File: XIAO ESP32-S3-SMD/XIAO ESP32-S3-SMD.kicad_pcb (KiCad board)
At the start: 2 copper layers, 12 parts, among them J1 Conn_01x04_Socket, J2 Conn_01x03_Socket, J3 Conn_01x04_Socket, J4 Conn_01x03_Socket, J5 Conn_01x03_Socket, J6 Conn_01x02_Pin, U2 XIAO-ESP32-S3-SMD

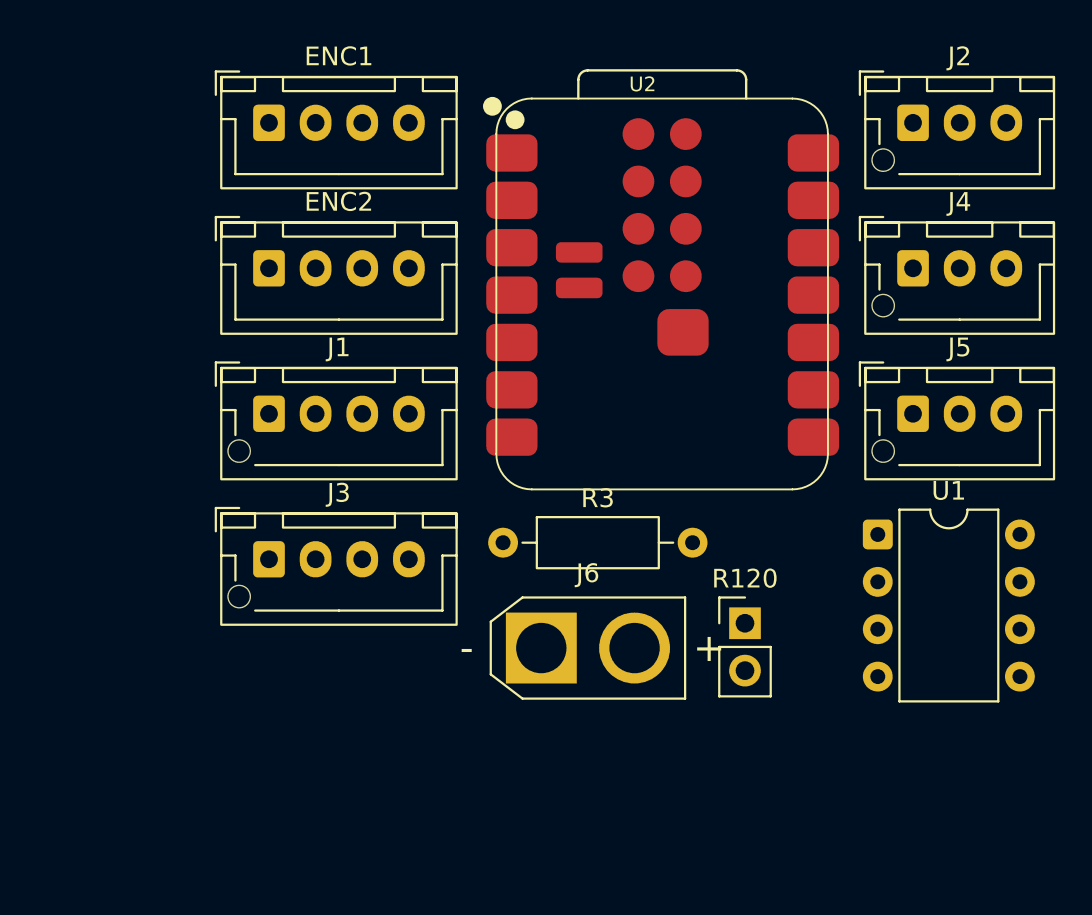
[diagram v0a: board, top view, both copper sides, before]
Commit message: XIAO S3の配置、配線前
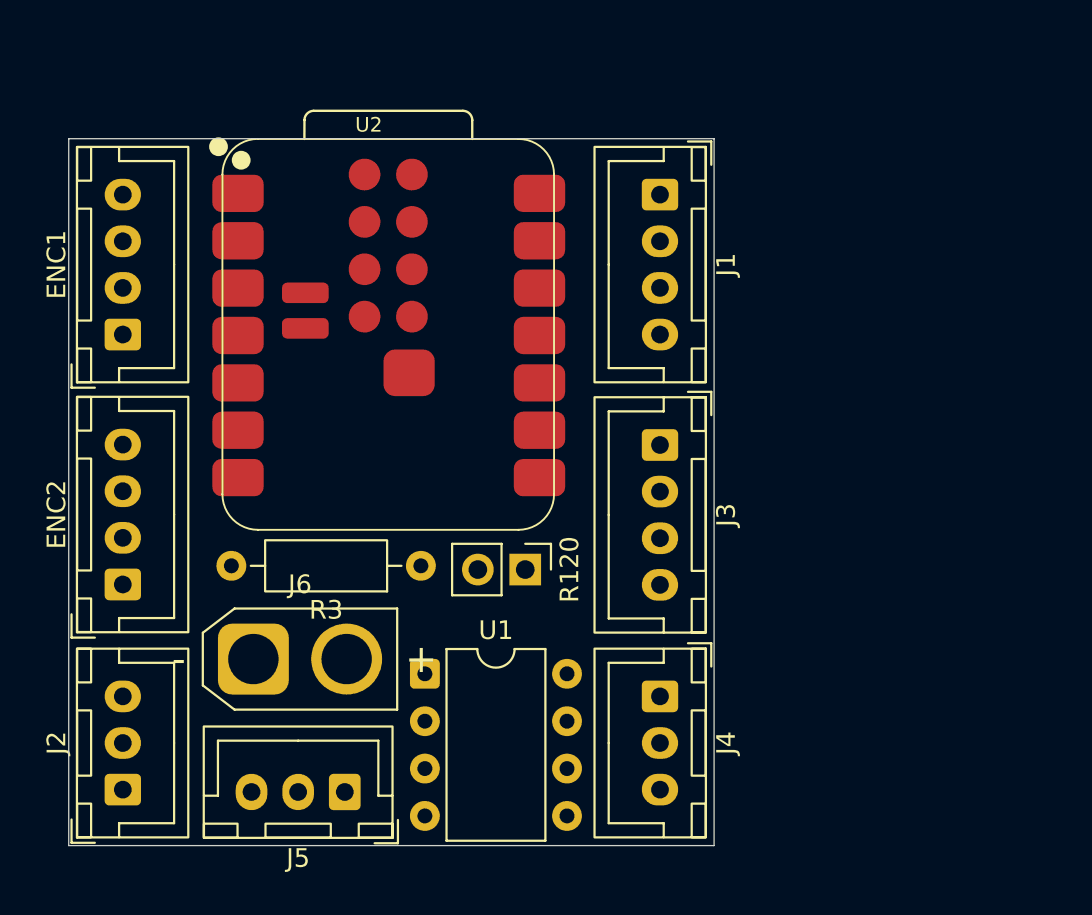
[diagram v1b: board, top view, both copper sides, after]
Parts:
- J1, J3: footprint Connector_JST:JST_XH_B4B-XH-AM_1x04_P2.50mm_Vertical -> Connector_JST:JST_XH_B4B-XH-A_1x04_P2.50mm_Vertical
- J2, J4, J5: footprint Connector_JST:JST_XH_B3B-XH-AM_1x03_P2.50mm_Vertical -> Connector_JST:JST_XH_B3B-XH-A_1x03_P2.50mm_Vertical
- moved J2 55.4 mm to (135.6, 97.3), turned to 90 degrees
- moved J5 36.6 mm to (147.5, 97.4), turned to 180 degrees
- moved J4 26.7 mm to (164.4, 92.3), turned to -90 degrees
- moved U1 25.4 mm to (151.8, 91.1)
- moved J1 24.0 mm to (164.4, 65.4), turned to -90 degrees
- moved J3 21.8 mm to (164.4, 78.8), turned to -90 degrees
- moved ENC2 18.7 mm to (135.6, 86.3), turned to 90 degrees
- moved J6 15.4 mm to (142.6, 90.3)
- moved U2 14.8 mm to (140.9, 83.5)
- moved ENC1 13.8 mm to (135.6, 72.9), turned to 90 degrees
- moved R120 12.1 mm to (157.2, 85.5), turned to -90 degrees
- moved R3 4.58 mm to (151.6, 85.3), turned to 180 degrees
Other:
- board outline added: 34.6 x 37.9 mm

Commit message: 電源ライン配線前
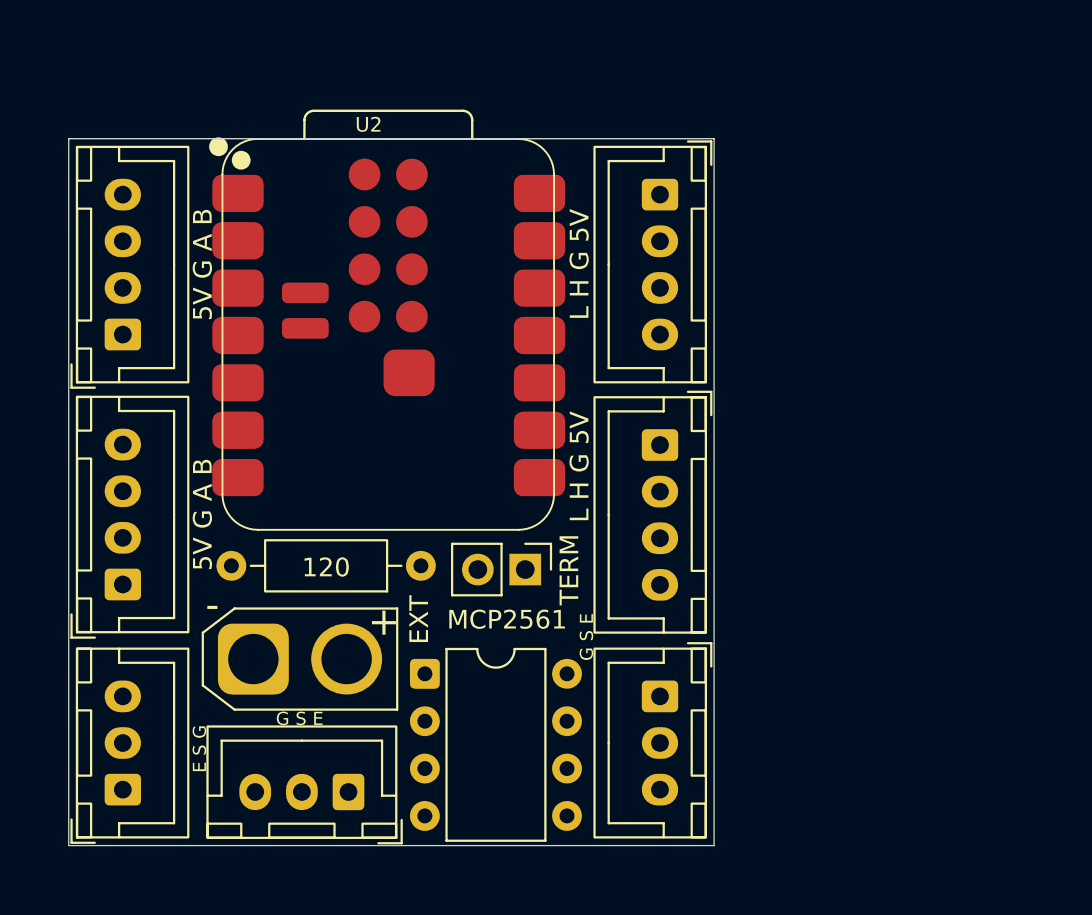
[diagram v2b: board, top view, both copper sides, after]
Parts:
- 5V G A B: renamed from ENC2
- 5V G A B: renamed from ENC1
- E S G: renamed from J2
- G S E: renamed from J5
- G S E: renamed from J4
- L H G 5V: renamed from J3
- L H G 5V: renamed from J1
- moved G S E 0.20 mm to (147.7, 97.4)
- renumbered R3 to 120, J6 to EXT, U1 to MCP2561, R120 to TERM
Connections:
- EXT pad 1: EXT_POWER -> GND
- EXT pad 2: GND -> EXT_POWER
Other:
- board text added: "CAN"
- board text added: "E S G"
- board text added: "ENC1"
- board text added: "ENC2"
- board text added: "G S E"
- board text added: "MULTI1"
- board text added: "MULTI2"
- board text added: "MULTI3"
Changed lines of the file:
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@@
 		(descr "8-lead though-hole mounted DIP package, row spacing 7.62mm (300 mils)")
 		(tags "THT DIP DIL PDIP 2.54mm 7.62mm 300mil")
-		(property "Reference" "U1"
-			(at 3.81 -2.33 0)
+		(property "Reference" "MCP2561"
+			(at 4.405 -2.89 0)
 			(layer "F.SilkS")
 			(effects
@@
 		(descr "Through hole straight pin header, 1x02, 2.54mm pitch, single row")
 		(tags "Through hole pin header THT 1x02 2.54mm single row")
-		(property "Reference" "R120"
+		(property "Reference" "TERM"
 			(at 0 -2.38 90)
 			(layer "F.SilkS")
@@
 		(descr "Connector XT30 Vertical Cable Male, https://www.tme.eu/Document/7d9d972ae3468777f69ec2ee99897652/XT30U-M.pdf")
 		(tags "RC Connector XT30")
-		(property "Reference" "J6"
-			(at 2.5 -4 0)
-			(layer "F.SilkS")
+		(property "Reference" "EXT"
+			(at 8.9 -2.1 90)
+			(layer "F.SilkS" knockout)
 			(effects
 				(font
@@
 		)
 		(fp_text user "-"
-			(at -4 0 0)
+			(at -2.2 -2.9 0)
 			(layer "F.SilkS")
 			(effects
@@
 		)
 		(fp_text user "+"
-			(at 9 0 0)
+			(at 7 -2 0)
 			(layer "F.SilkS")
 			(effects
@@
 			(remove_unused_layers no)
 			(roundrect_rratio 0.2)
-			(net "EXT_POWER")
+			(net "GND")
 			(pinfunction "Pin_1_1")
 			(pintype "passive")
@@
 			(layers "*.Cu" "*.Mask")
 			(remove_unused_layers no)
-			(net "GND")
+			(net "EXT_POWER")
 			(pinfunction "Pin_2_2")
 			(pintype "passive")
@@
 		(descr "JST XH series connector, B4B-XH-A (http://www.jst-mfg.com/product/pdf/eng/eXH.pdf)")
 		(tags "connector JST XH vertical")
-		(property "Reference" "J3"
-			(at 3.75 -3.55 90)
-			(layer "F.SilkS")
+		(property "Reference" "L H G 5V"
+			(at 1.17875 4.3 90)
+			(layer "F.SilkS" knockout)
 			(effects
 				(font
@@
 		(descr "JST XH series connector, B4B-XH-A (http://www.jst-mfg.com/product/pdf/eng/eXH.pdf)")
 		(tags "connector JST XH vertical")
-		(property "Reference" "ENC2"
-			(at 3.75 -3.55 90)
-			(layer "F.SilkS")
+		(property "Reference" "5V G A B"
+			(at 3.75 4.3 90)
+			(layer "F.SilkS" knockout)
 			(effects
 				(font
@@
 		(descr "JST XH series connector, B4B-XH-A (http://www.jst-mfg.com/product/pdf/eng/eXH.pdf)")
 		(tags "connector JST XH vertical")
-		(property "Reference" "J1"
-			(at 3.75 -3.55 90)
-			(layer "F.SilkS")
+		(property "Reference" "L H G 5V"
+			(at 3.75 4.3 90)
+			(layer "F.SilkS" knockout)
 			(effects
 				(font
@@
 		(descr "JST XH series connector, B4B-XH-A (http://www.jst-mfg.com/product/pdf/eng/eXH.pdf)")
 		(tags "connector JST XH vertical")
-		(property "Reference" "ENC1"
-			(at 3.75 -3.55 90)
-			(layer "F.SilkS")
+		(property "Reference" "5V G A B"
+			(at 3.75 4.3 90)
+			(layer "F.SilkS" knockout)
 			(effects
 				(font
@@
 	(footprint "Connector_JST:JST_XH_B3B-XH-A_1x03_P2.50mm_Vertical"
 		(layer "F.Cu")
-		(at 147.5 97.425 180)
+		(at 147.7 97.425 180)
 		(descr "JST XH series connector, B3B-XH-A (http://www.jst-mfg.com/product/pdf/eng/eXH.pdf)")
 		(tags "connector JST XH vertical")
-		(property "Reference" "J5"
-			(at 2.5 -3.55 0)
-			(layer "F.SilkS")
+		(property "Reference" "G S E"
+			(at 2.5 1.725 0)
+			(layer "F.SilkS" knockout)
+			(hide yes)
 			(effects
 				(font
@@
 		(descr "Resistor, Axial_DIN0207 series, Axial, Horizontal, pin pitch=10.16mm, 0.25W = 1/4W, length*diameter=6.3*2.5mm^2, http://cdn-reichelt.de/documents/datenblatt/B400/1_4W%23YAG.pdf")
 		(tags "Resistor Axial_DIN0207 series Axial Horizontal pin pitch 10.16mm 0.25W = 1/4W length 6.3mm diameter 2.5mm")
-		(property "Reference" "R3"
-			(at 5.08 -2.37 0)
+		(property "Reference" "120"
+			(at 5.08 -0.1 0)
 			(layer "F.SilkS")
 			(effects
@@
 		(descr "JST XH series connector, B3B-XH-A (http://www.jst-mfg.com/product/pdf/eng/eXH.pdf)")
 		(tags "connector JST XH vertical")
-		(property "Reference" "J4"
-			(at 2.5 -3.55 90)
-			(layer "F.SilkS")
+		(property "Reference" "G S E"
+			(at 2.5 1.8 90)
+			(layer "F.SilkS" knockout)
+			(hide yes)
 			(effects
 				(font
@@
 		(descr "JST XH series connector, B3B-XH-A (http://www.jst-mfg.com/product/pdf/eng/eXH.pdf)")
 		(tags "connector JST XH vertical")
-		(property "Reference" "J2"
-			(at 2.5 -3.55 90)
-			(layer "F.SilkS")
+		(property "Reference" "E S G"
+			(at 2.7 1.9 90)
+			(layer "F.SilkS" knockout)
+			(hide yes)
 			(effects
 				(font
@@
 		(layer "Edge.Cuts")
 	)
+	(gr_text "G S E"
+		(at 143.8 93.915 0)
+		(layer "F.SilkS" knockout)
+		(effects
+			(font
+				(size 0.7 0.7)
+				(thickness 0.1)
+			)
+			(justify left bottom)
+		)
+	)
+	(gr_text "E S G"
+		(at 140.14 96.4 90)
+		(layer "F.SilkS" knockout)
+		(effects
+			(font
+				(size 0.7 0.7)
+				(thickness 0.1)
+			)
+			(justify left bottom)
+		)
+	)
+	(gr_text "G S E"
+		(at 160.89 90.4 90)
+		(layer "F.SilkS" knockout)
+		(effects
+			(font
+				(size 0.7 0.7)
+				(thickness 0.1)
+			)
+			(justify left bottom)
+		)
+	)
+	(gr_text "MULTI3"
+		(at 145.3 95.7 0)
+		(layer "B.SilkS")
+		(effects
+			(font
+				(size 1 1)
+				(thickness 0.15)
+			)
+			(justify mirror)
+		)
+	)
+	(gr_text "MULTI1"
+		(at 137.4 94.5 90)
+		(layer "B.SilkS")
+		(effects
+			(font
+				(size 1 1)
+				(thickness 0.15)
+			)
+			(justify mirror)
+		)
+	)
+	(gr_text "ENC1"
+		(at 137.5 69.2 90)
+		(layer "B.SilkS")
+		(effects
+			(font
+				(size 1 1)
+				(thickness 0.15)
+			)
+			(justify mirror)
+		)
+	)
+	(gr_text "ENC2"
+		(at 137.6 82.5 90)
+		(layer "B.SilkS")
+		(effects
+			(font
+				(size 1 1)
+				(thickness 0.15)
+			)
+			(justify mirror)
+		)
+	)
+	(gr_text "CAN"
+		(at 162.6 69.1 90)
+		(layer "B.SilkS")
+		(effects
+			(font
+				(size 1 1)
+				(thickness 0.15)
+			)
+			(justify mirror)
+		)
+	)
+	(gr_text "CAN"
+		(at 162.6 82.4 90)
+		(layer "B.SilkS")
+		(effects
+			(font
+				(size 1 1)
+				(thickness 0.15)
+			)
+			(justify mirror)
+		)
+	)
+	(gr_text "MULTI2"
+		(at 162.6 94.8 90)
+		(layer "B.SilkS")
+		(effects
+			(font
+				(size 1 1)
+				(thickness 0.15)
+			)
+			(justify mirror)
+		)
+	)
 	(embedded_fonts no)

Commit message: 電源ラインの配線
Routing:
- net GND: track 0.00 -> 42.6 mm
- net EXT_POWER: track 0.00 -> 42.4 mm
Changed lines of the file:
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@@
 		)
 		(fp_text user "-"
-			(at -2.2 -2.9 0)
+			(at -2.4 -2.9 0)
 			(layer "F.SilkS")
 			(effects
@@
 		)
 	)
+	(segment
+		(start 137.6 90.3)
+		(end 135.6 92.3)
+		(width 2)
+		(layer "F.Cu")
+		(net "GND")
+	)
+	(segment
+		(start 142.6 90.3)
+		(end 137.6 90.3)
+		(width 2)
+		(layer "F.Cu")
+		(net "GND")
+	)
+	(segment
+		(start 142.73 93.63)
+		(end 142.7 93.6)
+		(width 2)
+		(layer "B.Cu")
+		(net "GND")
+	)
+	(segment
+		(start 151.795 93.63)
+		(end 142.73 93.63)
+		(width 2)
+		(layer "B.Cu")
+		(net "GND")
+	)
+	(segment
+		(start 164.4 97.3)
+		(end 162.8 97.3)
+		(width 2)
+		(layer "B.Cu")
+		(net "GND")
+	)
+	(segment
+		(start 142.7 93.6)
+		(end 142.7 90.4)
+		(width 2)
+		(layer "B.Cu")
+		(net "GND")
+	)
+	(segment
+		(start 158.91 91.09)
+		(end 156.37 93.63)
+		(width 2)
+		(layer "B.Cu")
+		(net "GND")
+	)
+	(segment
+		(start 142.7 97.425)
+		(end 142.7 93.6)
+		(width 2)
+		(layer "B.Cu")
+		(net "GND")
+	)
+	(segment
+		(start 142.7 90.4)
+		(end 142.6 90.3)
+		(width 0.2)
+		(layer "B.Cu")
+		(net "GND")
+	)
+	(segment
+		(start 160.54637 91.09)
+		(end 159.415 91.09)
+		(width 2)
+		(layer "B.Cu")
+		(net "GND")
+	)
+	(segment
+		(start 159.415 91.09)
+		(end 158.91 91.09)
+		(width 2)
+		(layer "B.Cu")
+		(net "GND")
+	)
+	(segment
+		(start 162.8 97.3)
+		(end 162.1 96.6)
+		(width 2)
+		(layer "B.Cu")
+		(net "GND")
+	)
+	(segment
+		(start 156.37 93.63)
+		(end 151.795 93.63)
+		(width 2)
+		(layer "B.Cu")
+		(net "GND")
+	)
+	(segment
+		(start 162.1 96.6)
+		(end 162.1 92.64363)
+		(width 2)
+		(layer "B.Cu")
+		(net "GND")
+	)
+	(segment
+		(start 162.1 92.64363)
+		(end 160.54637 91.09)
+		(width 2)
+		(layer "B.Cu")
+		(net "GND")
+	)
+	(segment
+		(start 135.6 97.3)
+		(end 137.7 97.3)
+		(width 2)
+		(layer "F.Cu")
+		(net "EXT_POWER")
+	)
+	(segment
+		(start 147.7 97.425)
+		(end 147.7 90.4)
+		(width 2)
+		(layer "F.Cu")
+		(net "EXT_POWER")
+	)
+	(segment
+		(start 147.7 90.4)
+		(end 147.6 90.3)
+		(width 0.2)
+		(layer "F.Cu")
+		(net "EXT_POWER")
+	)
+	(segment
+		(start 141.3 93.7)
+		(end 146.1 93.7)
+		(width 2)
+		(layer "F.Cu")
+		(net "EXT_POWER")
+	)
+	(segment
+		(start 147.7 90.4)
+		(end 149.8 88.3)
+		(width 2)
+		(layer "F.Cu")
+		(net "EXT_POWER")
+	)
+	(segment
+		(start 137.7 97.3)
+		(end 141.3 93.7)
+		(width 2)
+		(layer "F.Cu")
+		(net "EXT_POWER")
+	)
+	(segment
+		(start 146.1 93.7)
+		(end 147.6 92.2)
+		(width 2)
+		(layer "F.Cu")
+		(net "EXT_POWER")
+	)
+	(segment
+		(start 147.6 92.2)
+		(end 147.6 90.3)
+		(width 0.2)
+		(layer "F.Cu")
+		(net "EXT_POWER")
+	)
+	(segment
+		(start 160.4 88.3)
+		(end 164.4 92.3)
+		(width 2)
+		(layer "F.Cu")
+		(net "EXT_POWER")
+	)
+	(segment
+		(start 149.8 88.3)
+		(end 160.4 88.3)
+		(width 2)
+		(layer "F.Cu")
+		(net "EXT_POWER")
+	)
 	(embedded_fonts no)

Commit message: 一晩寝かせよう
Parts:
- added G***: LOGO, LOGO, B.Cu at (154.6, 77.6)
- added G***: LOGO, LOGO, B.Cu at (146.2, 77.5)
- added soki: LOGO, LOGO, B.Cu at (149.2, 67.2)
- CAN1, CAN2: renamed from L H G 5V
- ENC1, ENC2: renamed from 5V G A B
- ESG1: renamed from E S G
- GSE2, GSE3: renamed from G S E
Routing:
- net 5V0: track 0.00 -> 101.8 mm
- net CAN_TX: track 0.00 -> 60.7 mm
- net CAN_RX: track 0.00 -> 60.2 mm
- net CANL: track 0.00 -> 59.8 mm, vias 0 -> 2
- net GPIO9: track 0.00 -> 45.3 mm, vias 0 -> 2
- net CANH: track 0.00 -> 40.9 mm, vias 0 -> 1
- net GPIO7: track 0.00 -> 40.5 mm, vias 0 -> 2
- net GPIO8: track 0.00 -> 28.8 mm, vias 0 -> 2
- net ENC1_B: track 0.00 -> 11.5 mm, vias 0 -> 2
- net ENC2_A: track 0.00 -> 9.89 mm, vias 0 -> 2
- net ENC1_A: track 0.00 -> 7.22 mm, vias 0 -> 2
- net ENC2_B: track 0.00 -> 6.69 mm, vias 0 -> 2
- net Net-(R120-Pin_2): track 0.00 -> 3.14 mm
- added copper zone on B.Cu, net GND
- added copper zone on F.Cu, net GND
